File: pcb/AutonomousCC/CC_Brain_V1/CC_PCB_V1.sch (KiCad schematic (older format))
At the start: 14 parts, among them J1 Screw_Terminal_01x07, J2 Antenna_Conn_02x04_Odd_Even, J3 USB1130-15-A_REVA, J5 Relay_Conn_01x06, U1 Pico, U2 LM337_TO3

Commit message: Added Switch for Pico Programming
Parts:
- added S1: SSA12G, my_footprints:SW_SSA12G, symbol SSA12G:SSA12G
- C1: symbol Device:CP -> CC_PCB_V1-rescue:CP-Device
- C2: symbol Device:C -> CC_PCB_V1-rescue:C-Device
- H1, H2, H3, H4: symbol Mechanical:MountingHole -> CC_PCB_V1-rescue:MountingHole-Mechanical
- J1: symbol Connector:Screw_Terminal_01x07 -> CC_PCB_V1-rescue:Screw_Terminal_01x07-Connector
- J2: symbol Connector_Generic:Conn_02x04_Odd_Even -> CC_PCB_V1-rescue:Conn_02x04_Odd_Even-Connector_Generic
- J5: symbol Connector_Generic:Conn_01x06 -> CC_PCB_V1-rescue:Conn_01x06-Connector_Generic
- U2: symbol Regulator_Linear:LM337_TO3 -> CC_PCB_V1-rescue:LM337_TO3-Regulator_Linear
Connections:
- net labels added: +3.3V_Pico
- wire segments 25 -> 27
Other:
- note added: "Pico Power Switch for Programming\n"
- note added: "USB (PWR In)\n"
- moved on the sheet: J3, Screw_Terminal1, Screw_Terminal2

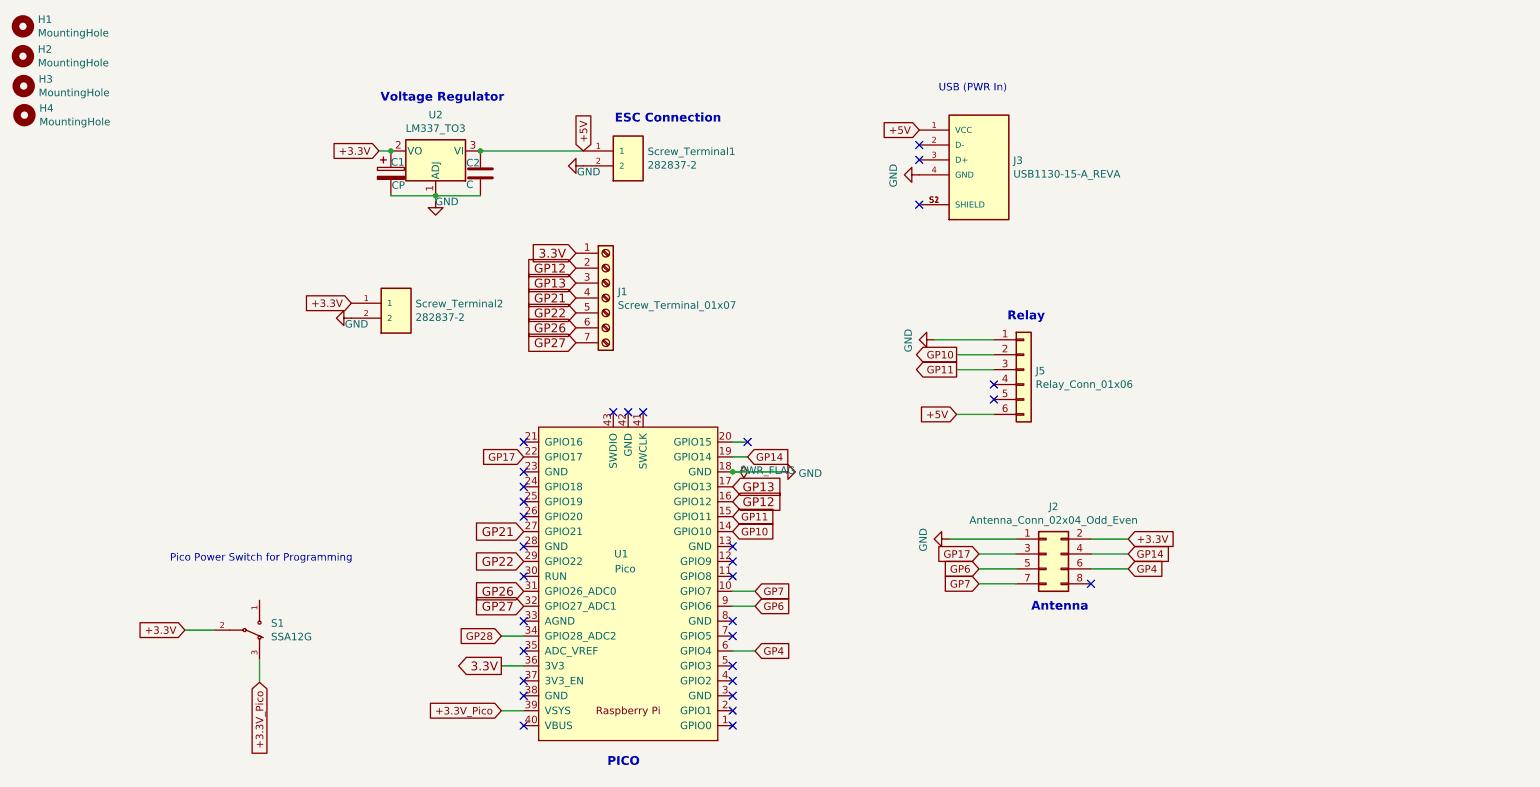
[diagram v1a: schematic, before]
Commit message: Updated Antenna CC_Brain Pins and Added Relay Circuit
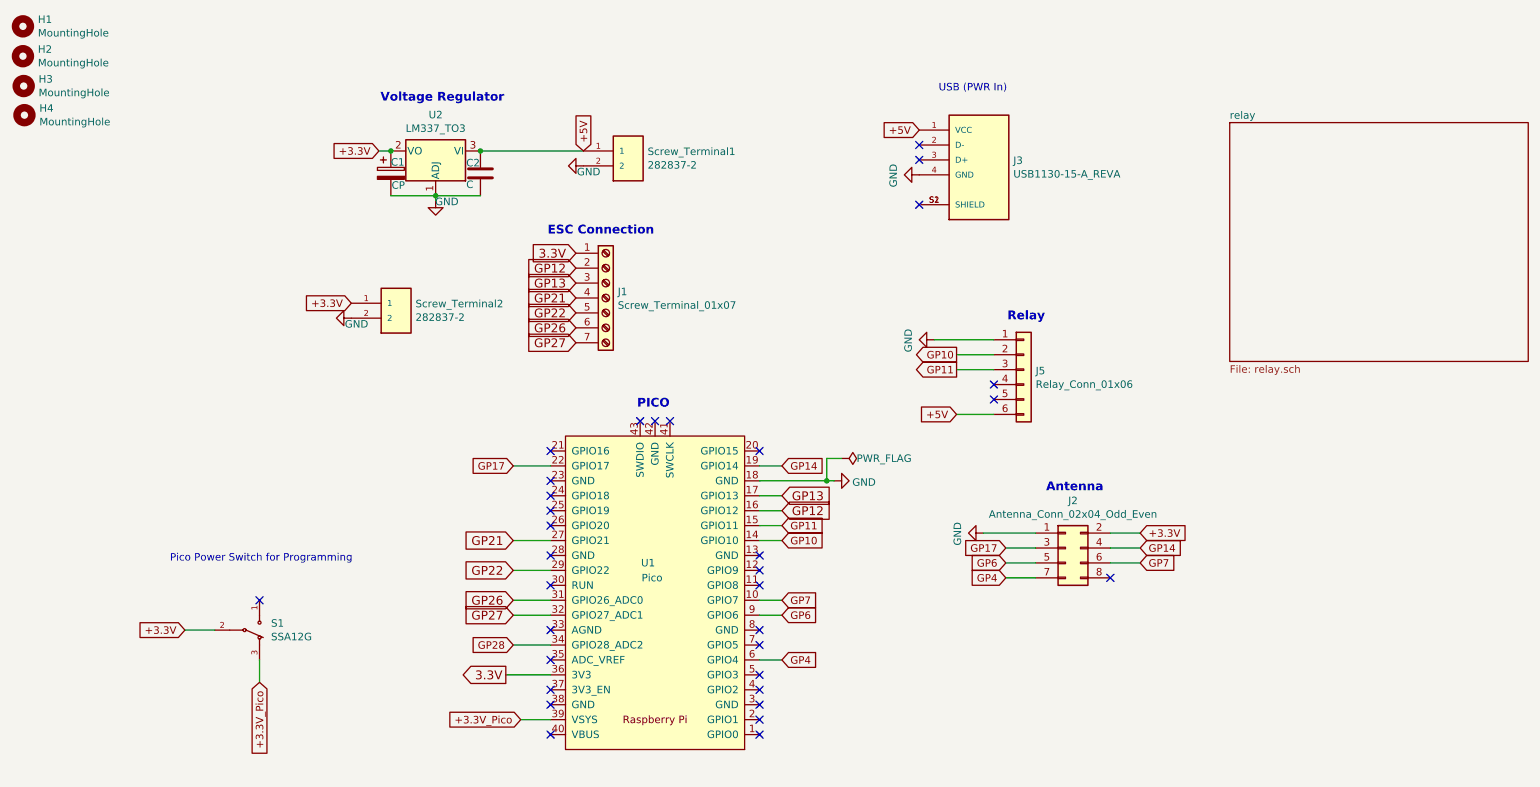
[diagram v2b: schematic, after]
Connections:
- net GP4: now also J2.7 (Pin_7); no longer J2.6 (Pin_6)
- net GP7: now also J2.6 (Pin_6); no longer J2.7 (Pin_7)
- no-connect marks 32 -> 33
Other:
- moved on the sheet: J2, U1
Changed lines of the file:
@@
 $Descr A4 11693 8268
 encoding utf-8
-Sheet 1 1
+Sheet 1 2
 Title "Autonomous Crazy Cart V1"
 Date "09/12/2021"
@@
 $EndDescr
 $Comp
-L CC_PCB_V1-rescue:Pico-MCU_RaspberryPi_and_Boards U1
-U 1 1 61312BD2
-P 4820 4440
-F 0 "U1" H 4820 4240 50  0000 L CNN
-F 1 "Pico" H 4770 4340 50  0000 L CNN
-F 2 "MCU_RaspberryPi_and_Boards:RPi_Pico_SMD_TH" V 4820 4440 50  0001 C CNN
-F 3 "" H 4820 4440 50  0001 C CNN
-	1    4820 4440
-	-1   0    0    1
-$EndComp
-$Comp
 L CC_PCB_V1-rescue:Conn_01x06-Connector_Generic J5
 U 1 1 6132C346
@@
 L CC_PCB_V1-rescue:Conn_02x04_Odd_Even-Connector_Generic J2
 U 1 1 6132E9AC
-P 7620 4240
-F 0 "J2" H 7670 4557 50  0000 C CNN
-F 1 "Antenna_Conn_02x04_Odd_Even" H 7670 4466 50  0000 C CNN
-F 2 "Connector_PinHeader_2.54mm:PinHeader_2x04_P2.54mm_Vertical" H 7620 4240 50  0001 C CNN
-F 3 "~" H 7620 4240 50  0001 C CNN
-	1    7620 4240
-	1    0    0    -1
-$EndComp
-Text GLabel 8170 4240 2    50   Input ~ 0
+P 7750 4200
+F 0 "J2" H 7800 4517 50  0000 C CNN
+F 1 "Antenna_Conn_02x04_Odd_Even" H 7800 4426 50  0000 C CNN
+F 2 "Connector_PinHeader_2.54mm:PinHeader_2x04_P2.54mm_Vertical" H 7750 4200 50  0001 C CNN
+F 3 "~" H 7750 4200 50  0001 C CNN
+	1    7750 4200
+	1    0    0    -1
+$EndComp
+Text GLabel 8250 4200 2    50   Input ~ 0
 GP14
-Text GLabel 5620 3590 2    50   Input ~ 0
+Text GLabel 5850 3650 2    50   Input ~ 0
 GP14
-Text GLabel 7170 4240 0    50   Input ~ 0
+Text GLabel 7350 4200 0    50   Input ~ 0
 GP17
 Wire Wire Line
@@
 Wire Wire Line
 	7020 3005 7270 3005
-Wire Wire Line
-	7920 4240 8170 4240
-Wire Wire Line
-	7170 4240 7420 4240
-Wire Wire Line
-	5620 3490 5520 3490
-Wire Wire Line
-	5520 3590 5620 3590
 $Comp
 L CC_PCB_V1-rescue:GND-power #PWR0102
 U 1 1 6139949D
-P 6970 4140
-F 0 "#PWR0102" H 6970 3890 50  0001 C CNN
-F 1 "GND" H 6975 3967 50  0000 C CNN
-F 2 "" H 6970 4140 50  0001 C CNN
-F 3 "" H 6970 4140 50  0001 C CNN
-	1    6970 4140
-	0    1    1    0
-$EndComp
-Wire Wire Line
-	7420 4140 6970 4140
-Text GLabel 5670 4890 2    50   Input ~ 0
+P 7200 4100
+F 0 "#PWR0102" H 7200 3850 50  0001 C CNN
+F 1 "GND" H 7205 3927 50  0000 C CNN
+F 2 "" H 7200 4100 50  0001 C CNN
+F 3 "" H 7200 4100 50  0001 C CNN
+	1    7200 4100
+	0    1    1    0
+$EndComp
+Text GLabel 5850 4950 2    50   Input ~ 0
 GP4
-Wire Wire Line
-	7420 4440 7170 4440
-Wire Wire Line
-	5520 4890 5670 4890
-Text GLabel 5670 4590 2    50   Input ~ 0
+Text GLabel 5850 4650 2    50   Input ~ 0
 GP6
-Text GLabel 5670 4490 2    50   Input ~ 0
+Text GLabel 5850 4550 2    50   Input ~ 0
 GP7
-Text GLabel 7170 4340 0    50   Input ~ 0
+Text GLabel 7350 4300 0    50   Input ~ 0
 GP6
-Text GLabel 7170 4440 0    50   Input ~ 0
+Text GLabel 8250 4300 2    50   Input ~ 0
 GP7
-Wire Wire Line
-	8170 4340 7920 4340
-Wire Wire Line
-	7420 4340 7170 4340
-Wire Wire Line
-	5520 4590 5670 4590
 $Comp
 L CC_PCB_V1-rescue:GND-power #PWR0105
@@
 Wire Wire Line
 	7270 3305 7020 3305
-Text GLabel 8170 4340 2    50   Input ~ 0
+Text GLabel 7350 4400 0    50   Input ~ 0
 GP4
-NoConn ~ 5520 5390
-NoConn ~ 5520 5290
-NoConn ~ 5520 5190
-NoConn ~ 5520 5090
-NoConn ~ 5520 4990
-NoConn ~ 5520 4790
-NoConn ~ 5520 4690
-NoConn ~ 5520 4390
-NoConn ~ 5520 4290
-NoConn ~ 5520 4190
-NoConn ~ 4120 5390
-NoConn ~ 4120 5090
-NoConn ~ 4120 4890
-NoConn ~ 4120 4690
-NoConn ~ 4120 4390
-NoConn ~ 4120 4190
-NoConn ~ 4120 3990
-NoConn ~ 4120 3890
-NoConn ~ 4120 3790
-NoConn ~ 4120 3690
-NoConn ~ 4720 3290
-NoConn ~ 4820 3290
-NoConn ~ 4920 3290
-NoConn ~ 7920 4440
 NoConn ~ 7270 3205
 NoConn ~ 7270 3105
-Text Notes 7520 4630 0    59   ~ 12
+Text Notes 7620 3830 0    59   ~ 12
 Antenna
 Text Notes 7360 2685 0    59   ~ 12
 Relay
-Text Notes 4680 5670 0    59   ~ 12
+Text Notes 4880 3270 0    59   ~ 12
 PICO
-Text Notes 4730 1360 0    59   ~ 12
+Text Notes 4280 2110 0    59   ~ 12
 ESC Connection
 $Comp
 L CC_PCB_V1-rescue:GND-power #PWR0101
 U 1 1 6132D47F
-P 5840 3690
-F 0 "#PWR0101" H 5840 3440 50  0001 C CNN
-F 1 "GND" V 5830 3490 50  0000 C CNN
-F 2 "" H 5840 3690 50  0001 C CNN
-F 3 "" H 5840 3690 50  0001 C CNN
-	1    5840 3690
+P 6200 3750
+F 0 "#PWR0101" H 6200 3500 50  0001 C CNN
+F 1 "GND" V 6190 3550 50  0000 C CNN
+F 2 "" H 6200 3750 50  0001 C CNN
+F 3 "" H 6200 3750 50  0001 C CNN
+	1    6200 3750
 	0    -1   -1   0
 $EndComp
@@
 L CC_PCB_V1-rescue:PWR_FLAG-power #FLG0103
 U 1 1 6132C74E
-P 5520 3690
-F 0 "#FLG0103" H 5520 3765 50  0001 C CNN
-F 1 "PWR_FLAG" V 5510 3740 50  0000 L CNN
-F 2 "" H 5520 3690 50  0001 C CNN
-F 3 "~" H 5520 3690 50  0001 C CNN
-	1    5520 3690
-	0    1    1    0
-$EndComp
-Wire Wire Line
-	5520 3690 5840 3690
-NoConn ~ 4120 5190
-Text GLabel 3970 4790 0    50   Input ~ 0
+P 6250 3600
+F 0 "#FLG0103" H 6250 3675 50  0001 C CNN
+F 1 "PWR_FLAG" V 6250 3700 50  0000 L CNN
+F 2 "" H 6250 3600 50  0001 C CNN
+F 3 "~" H 6250 3600 50  0001 C CNN
+	1    6250 3600
+	0    1    1    0
+$EndComp
+Text GLabel 4050 4850 0    50   Input ~ 0
 GP28
 $Comp
@@
 	0    1    1    0
 $EndComp
-Text GLabel 3970 5290 0    50   Input ~ 0
+Text GLabel 4100 5350 0    50   Input ~ 0
 +3.3V_Pico
 Text GLabel 7020 3305 0    50   Input ~ 0
 +5V
-Wire Wire Line
-	7920 4140 8170 4140
-Text GLabel 8170 4140 2    50   Input ~ 0
+Text GLabel 8250 4100 2    50   Input ~ 0
 +3.3V
-NoConn ~ 4120 3490
 Text GLabel 7020 2905 0    50   Output ~ 0
 GP10
 Text GLabel 7020 3005 0    50   Output ~ 0
 GP11
-Wire Wire Line
-	5670 4490 5520 4490
-Wire Wire Line
-	4120 4790 3970 4790
-Wire Wire Line
-	4120 5290 3970 5290
 Text GLabel 4520 1540 1    50   Input ~ 0
 +5V
@@
 Text Notes 3160 1220 0    59   ~ 12
 Voltage Regulator
-Connection ~ 5520 3690
-Text GLabel 3970 4990 0    59   Output ~ 0
+Text GLabel 4000 5050 0    59   Output ~ 0
 3.3V
 Text GLabel 4470 2225 0    59   Input ~ 0
 3.3V
-Wire Wire Line
-	4120 4990 3970 4990
 Text GLabel 4470 2325 0    59   Input ~ 0
 GP12
@@
 Text GLabel 4470 2825 0    59   Input ~ 0
 GP27
-Text GLabel 5520 3890 2    59   Input ~ 0
+Text GLabel 5850 3950 2    59   Input ~ 0
 GP12
-Text GLabel 5520 3790 2    59   Input ~ 0
+Text GLabel 5850 3850 2    59   Input ~ 0
 GP13
-Text GLabel 4120 4090 0    59   Input ~ 0
+Text GLabel 4050 4150 0    59   Input ~ 0
 GP21
-Text GLabel 4120 4290 0    59   Input ~ 0
+Text GLabel 4050 4350 0    59   Input ~ 0
 GP22
-Text GLabel 4120 4490 0    59   Input ~ 0
+Text GLabel 4050 4550 0    59   Input ~ 0
 GP26
-Text GLabel 4120 4590 0    59   Input ~ 0
+Text GLabel 4050 4650 0    59   Input ~ 0
 GP27
 $Comp
@@
 	3830 1540 4520 1540
 Connection ~ 3830 1540
-Text GLabel 5520 4090 2    50   Input ~ 0
-GP10
-Text GLabel 5520 3990 2    50   Input ~ 0
-GP11
-NoConn ~ 5620 3490
-Text GLabel 4120 3590 0    50   Input ~ 0
+Text GLabel 4050 3650 0    50   Input ~ 0
 GP17
 $Comp
@@
 Wire Wire Line
 	2350 4950 2350 5100
+$Sheet
+S 8850 1350 2000 1600
+U 615DA4AF
+F0 "relay" 50
+F1 "relay.sch" 50
+$EndSheet
+Text GLabel 5850 4150 2    50   Input ~ 0
+GP10
+Text GLabel 5850 4050 2    50   Input ~ 0
+GP11
+$Comp
+L CC_PCB_V1-rescue:Pico-MCU_RaspberryPi_and_Boards U1
+U 1 1 61312BD2
+P 5000 4500
+F 0 "U1" H 5000 4300 50  0000 L CNN
+F 1 "Pico" H 4950 4400 50  0000 L CNN
+F 2 "MCU_RaspberryPi_and_Boards:RPi_Pico_SMD_TH" V 5000 4500 50  0001 C CNN
+F 3 "" H 5000 4500 50  0001 C CNN
+	1    5000 4500
+	-1   0    0    1
+$EndComp
+Wire Wire Line
+	7350 4200 7550 4200
+Wire Wire Line
+	7550 4100 7200 4100
+Wire Wire Line
+	7350 4300 7550 4300
+Wire Wire Line
+	7550 4400 7350 4400
+Wire Wire Line
+	8050 4300 8250 4300
+Wire Wire Line
+	8250 4200 8050 4200
+Wire Wire Line
+	8050 4100 8250 4100
+Wire Wire Line
+	5850 3650 5700 3650
+Wire Wire Line
+	6200 3750 6150 3750
+Wire Wire Line
+	5700 3850 5850 3850
+Wire Wire Line
+	5850 3950 5700 3950
+Wire Wire Line
+	5700 4050 5850 4050
+Wire Wire Line
+	5850 4150 5700 4150
+Wire Wire Line
+	5700 4550 5850 4550
+Wire Wire Line
+	5850 4650 5700 4650
+Wire Wire Line
+	5850 4950 5700 4950
+Wire Wire Line
+	4300 4850 4050 4850
+Wire Wire Line
+	4050 4650 4300 4650
+Wire Wire Line
+	4300 4550 4050 4550
+Wire Wire Line
+	4050 4350 4300 4350
+Wire Wire Line
+	4300 4150 4050 4150
+Wire Wire Line
+	4050 3650 4300 3650
+Wire Wire Line
+	4100 5350 4300 5350
+Wire Wire Line
+	4000 5050 4300 5050
+Wire Wire Line
+	6250 3600 6150 3600
+Wire Wire Line
+	6150 3600 6150 3750
+Connection ~ 6150 3750
+Wire Wire Line
+	6150 3750 5700 3750
+NoConn ~ 2350 4550
+NoConn ~ 4300 5450
+NoConn ~ 4300 5250
+NoConn ~ 4300 5150
+NoConn ~ 4300 4950
+NoConn ~ 4300 4750
+NoConn ~ 4300 4450
+NoConn ~ 4300 4250
+NoConn ~ 4300 4050
+NoConn ~ 4300 3950
+NoConn ~ 4300 3850
+NoConn ~ 4300 3750
+NoConn ~ 4300 3550
+NoConn ~ 4900 3350
+NoConn ~ 5000 3350
+NoConn ~ 5100 3350
+NoConn ~ 5700 3550
+NoConn ~ 5700 4250
+NoConn ~ 5700 4350
+NoConn ~ 5700 4450
+NoConn ~ 5700 4750
+NoConn ~ 5700 4850
+NoConn ~ 5700 5050
+NoConn ~ 5700 5150
+NoConn ~ 5700 5250
+NoConn ~ 5700 5350
+NoConn ~ 5700 5450
+NoConn ~ 8050 4400
 $EndSCHEMATC

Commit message: Added Header Pin Connector
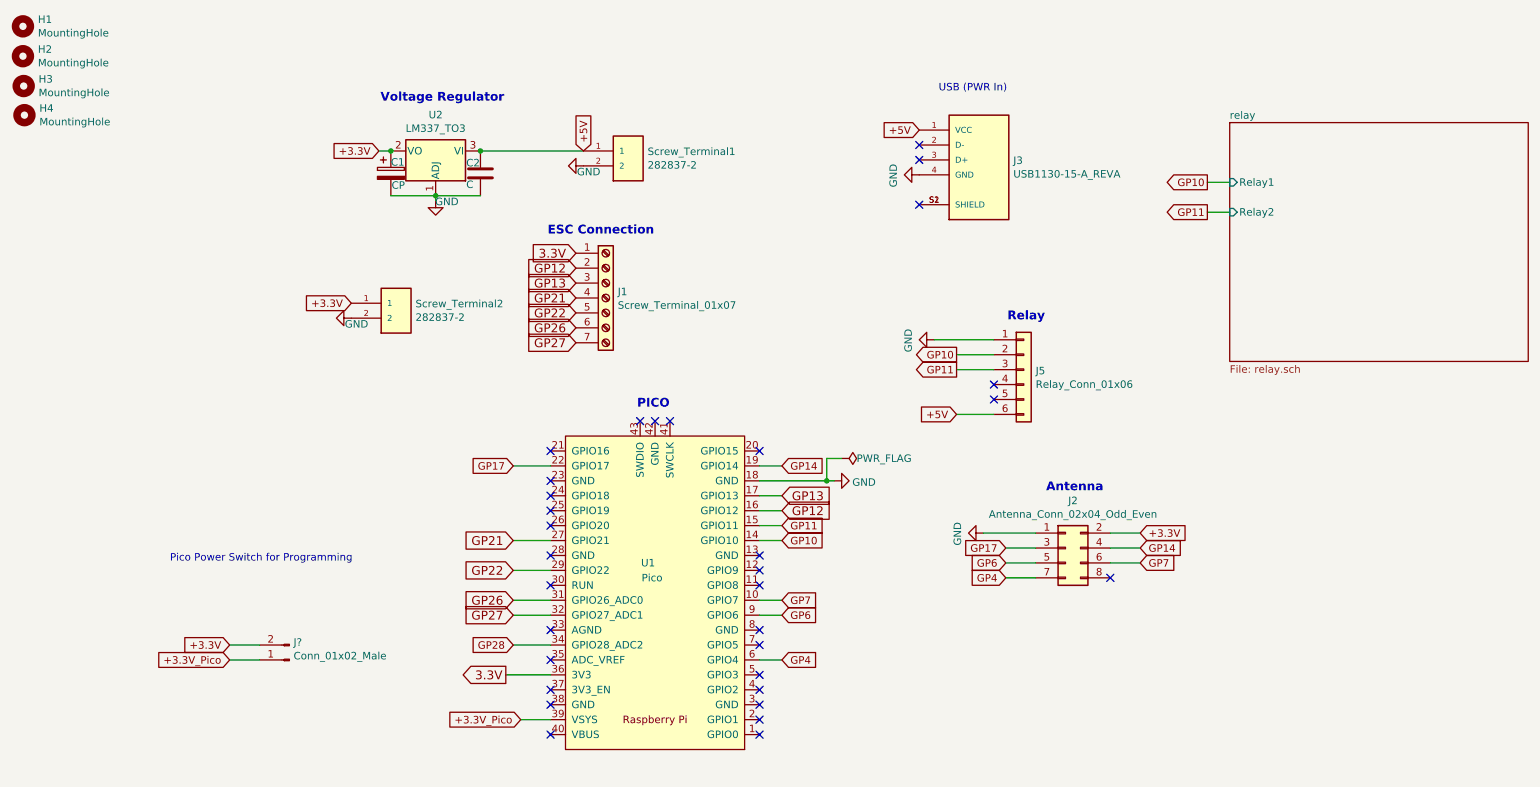
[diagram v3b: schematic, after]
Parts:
- removed S1: SSA12G, my_footprints:SW_SSA12G, symbol SSA12G:SSA12G
- added J?: Conn_01x02_Male, symbol Connector:Conn_01x02_Male
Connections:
- net +3.3V: now also J?.2 (Pin_2)
- net +3.3V_Pico: now also J?.1 (Pin_1)
- no-connect marks 33 -> 32
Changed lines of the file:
@@
 	1    0    0    -1
 $EndComp
-Text GLabel 2350 5100 3    50   Input ~ 0
+Text GLabel 2150 4950 0    50   Input ~ 0
 +3.3V_Pico
-Text GLabel 1850 4750 0    50   Input ~ 0
+Text GLabel 2150 4850 0    50   Input ~ 0
 +3.3V
 Text Notes 1750 4300 0    50   ~ 0
@@
 Text Notes 6900 1150 0    50   ~ 0
 USB (PWR In)\n
-$Comp
-L SSA12G:SSA12G S1
-U 1 1 615BBB5C
-P 2350 4750
-F 0 "S1" H 2427 4796 50  0000 L CNN
-F 1 "SSA12G" H 2427 4705 50  0000 L CNN
-F 2 "my_footprints:SW_SSA12G" H 2350 4750 50  0001 L BNN
-F 3 "" H 2350 4750 50  0001 L BNN
-F 4 "Compliant" H 2350 4750 50  0001 L BNN "EU_RoHS_Compliance"
-F 5 "1-1437575-5" H 2350 4750 50  0001 L BNN "Comment"
-	1    2350 4750
-	1    0    0    -1
-$EndComp
 Wire Wire Line
-	1850 4750 2050 4750
-Wire Wire Line
-	2350 4950 2350 5100
+	2150 4850 2350 4850
 $Sheet
 S 8850 1350 2000 1600
@@
 F0 "relay" 50
 F1 "relay.sch" 50
+F2 "Relay1" I L 8850 1750 50
+F3 "Relay2" I L 8850 1950 50
 $EndSheet
 Text GLabel 5850 4150 2    50   Input ~ 0
@@
 Wire Wire Line
 	6150 3750 5700 3750
-NoConn ~ 2350 4550
 NoConn ~ 4300 5450
 NoConn ~ 4300 5250
@@
 NoConn ~ 5700 5450
 NoConn ~ 8050 4400
+Wire Wire Line
+	8850 1750 8700 1750
+Wire Wire Line
+	8850 1950 8700 1950
+Text GLabel 8700 1750 0    50   Output ~ 0
+GP10
+Text GLabel 8700 1950 0    50   Output ~ 0
+GP11
+$Comp
+L Connector:Conn_01x02_Male J?
+U 1 1 61610430
+P 2550 4950
+F 0 "J?" H 2522 4832 50  0000 R CNN
+F 1 "Conn_01x02_Male" H 2522 4923 50  0000 R CNN
+F 2 "" H 2550 4950 50  0001 C CNN
+F 3 "~" H 2550 4950 50  0001 C CNN
+	1    2550 4950
+	-1   0    0    1
+$EndComp
+Wire Wire Line
+	2150 4950 2350 4950
 $EndSCHEMATC
